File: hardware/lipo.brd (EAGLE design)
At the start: 33.5 x 34.6 mm, 50 parts, among them J1 MICRO_USB_B_HIROSE_ZX62-B-5PA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, Q1 IRLML6402, Q2 IRLML6344, SW1 TVAF06-A020B-R, U1 LT6106CS5#PBF, U2 NJM12888F, X1 FA-238

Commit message: べたGND前です。esp32のschはノータッチなのでここに上がってないです。よろしくお願いします。
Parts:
- moved C10 0.25 mm to (3.56, -3.81)
- moved C6 0.25 mm to (0.51, -3.81)
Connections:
- net VDD: now also RP1.26
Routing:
- net VDD: track 73.1 -> 74.6 mm, vias 6 -> 7
- net GND: vias 71 -> 67

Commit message: 微修正
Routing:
- net GND: track 155.3 -> 175.0 mm

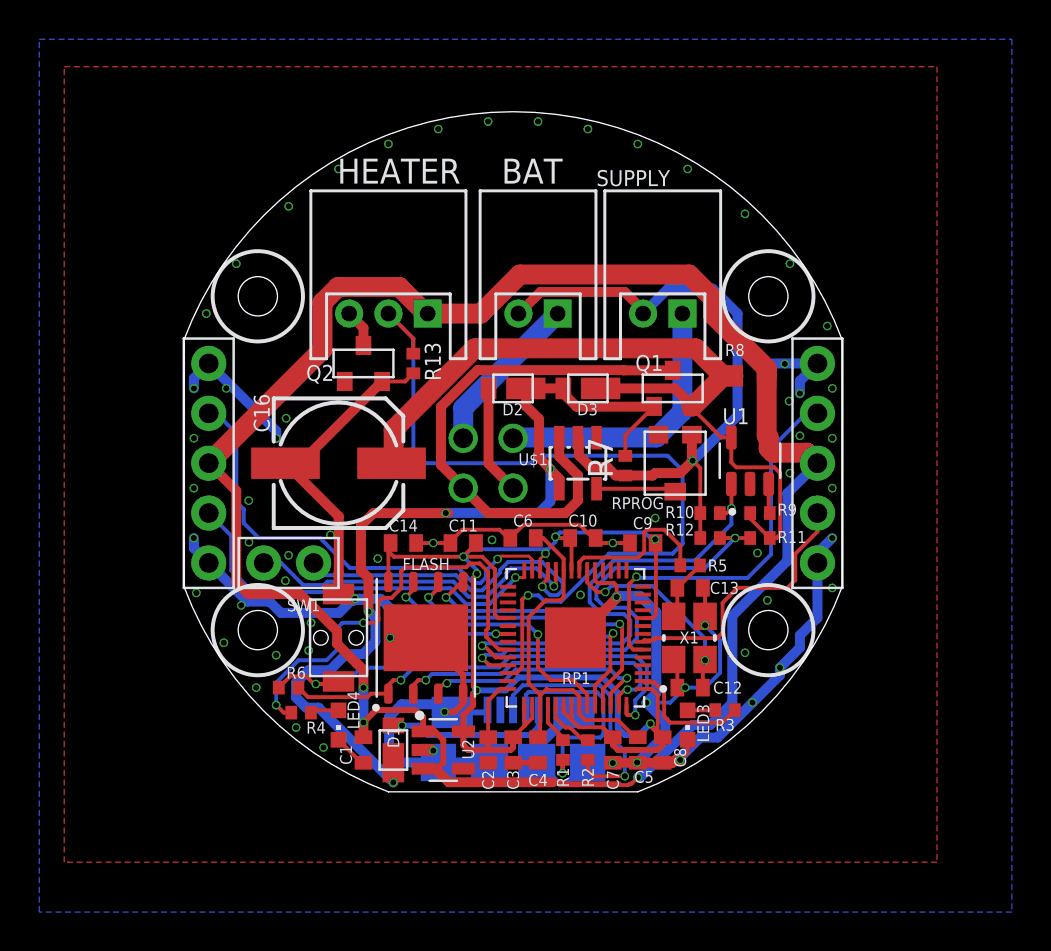
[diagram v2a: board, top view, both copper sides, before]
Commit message: シルクを調整
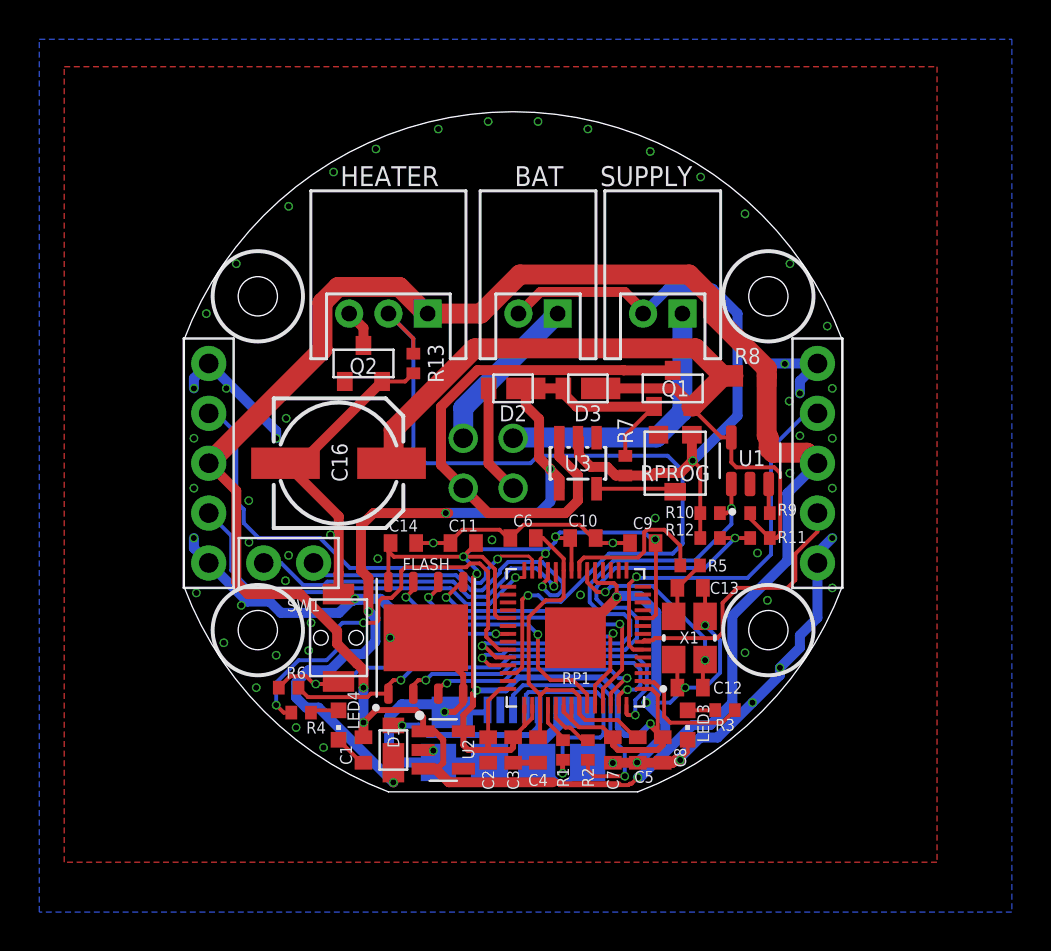
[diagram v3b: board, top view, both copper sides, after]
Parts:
- renumbered U$1 to U3
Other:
- board text added: "TERES LiPo Module"
- board text removed: "TERES Module"
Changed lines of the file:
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@@
 <layer number="27" name="tValues" color="7" fill="1" visible="yes" active="yes"/>
 <layer number="28" name="bValues" color="7" fill="1" visible="yes" active="yes"/>
-<layer number="29" name="tStop" color="7" fill="3" visible="no" active="yes"/>
-<layer number="30" name="bStop" color="7" fill="6" visible="no" active="yes"/>
+<layer number="29" name="tStop" color="7" fill="3" visible="yes" active="yes"/>
+<layer number="30" name="bStop" color="7" fill="6" visible="yes" active="yes"/>
 <layer number="31" name="tCream" color="7" fill="4" visible="no" active="yes"/>
 <layer number="32" name="bCream" color="7" fill="5" visible="no" active="yes"/>
@@
 <wire x1="-6.349996875" y1="-16.735815625" x2="-16.764" y2="-6.275209375" width="0" layer="20" curve="-48.699765"/>
 <wire x1="16.764" y1="-6.2752125" x2="6.35" y2="-16.7358125" width="0" layer="20" curve="-48.699745"/>
-<text x="0" y="14.859" size="1.27" layer="29" font="vector" ratio="10" align="center">2022 WASA Rocket</text>
-<text x="0" y="14.859" size="1.27" layer="30" font="vector" ratio="10" rot="MR0" align="center">TERES Module</text>
+<text x="0" y="16.002" size="1.016" layer="29" font="vector" ratio="10" align="center">2022 WASA Rocket</text>
+<text x="0.127" y="14.732" size="1.016" layer="30" font="vector" ratio="10" rot="MR0" align="center">TERES LiPo Module</text>
 <circle x="13" y="-8.5" radius="2.3" width="0.2" layer="22"/>
 <circle x="-13" y="-8.5" radius="2.3" width="0.2" layer="22"/>
@@
 <element name="U$2" library="pins" package="P2_2.54" value="P2_2_2.54" x="-11.43" y="-5.08" smashed="yes" rot="R90"/>
 <element name="BAT" library="jst-ph" package="S2B-PH-K-S" value="" x="1.27" y="7.62" smashed="yes">
-<attribute name="NAME" x="-0.587" y="14.239" size="1.27" layer="25" ratio="10"/>
+<attribute name="NAME" x="1.318" y="14.62" size="1.016" layer="25" font="vector" align="center"/>
 <attribute name="VALUE" x="-1.73" y="3.62" size="1.27" layer="27"/>
 </element>
-<element name="U$1" library="mcp73831" package="SOT23-5L" value="MCP73831" x="3.302" y="0" smashed="yes" rot="R180">
-<attribute name="NAME" x="1.778" y="0.508" size="0.6096" layer="25" font="vector" rot="R180"/>
+<element name="U3" library="mcp73831" package="SOT23-5L" value="MCP73831" x="3.302" y="0" smashed="yes" rot="R180">
+<attribute name="NAME" x="3.302" y="0" size="0.8128" layer="25" font="vector" rot="R180" align="center"/>
 </element>
 <element name="HEATER" library="jst-ph" package="S3B-PH-K-S" value="" x="-6.35" y="7.62" smashed="yes">
-<attribute name="NAME" x="-8.953" y="14.239" size="1.27" layer="25" ratio="10"/>
+<attribute name="NAME" x="-6.286" y="14.62" size="1.016" layer="25" font="vector" align="center"/>
 <attribute name="VALUE" x="-10.35" y="3.62" size="1.27" layer="27"/>
 </element>
 <element name="SUPPLY" library="jst-ph" package="S2B-PH-K-S" value="" x="7.62" y="7.62" smashed="yes">
-<attribute name="NAME" x="4.239" y="14.112" size="0.8128" layer="25" ratio="10"/>
+<attribute name="NAME" x="6.779" y="14.62" size="1.016" layer="25" font="vector" align="center"/>
 <attribute name="VALUE" x="4.62" y="3.62" size="1.27" layer="27"/>
 </element>
@@
 <attribute name="MF" value="Linear Technology" x="12.065" y="0.127" size="1.778" layer="27" rot="R90" display="off"/>
 <attribute name="MP" value="LT6106CS5#PBF" x="12.065" y="0.127" size="1.778" layer="27" rot="R90" display="off"/>
-<attribute name="NAME" x="12.033" y="2.799" size="0.8128" layer="25" rot="R180"/>
+<attribute name="NAME" x="12.16" y="0.259" size="0.8128" layer="25" font="vector" rot="R180" align="center"/>
 <attribute name="PACKAGE" value="TSOT-23 Linear Technology" x="12.065" y="0.127" size="1.778" layer="27" rot="R90" display="off"/>
 <attribute name="PRICE" value="None" x="12.065" y="0.127" size="1.778" layer="27" rot="R90" display="off"/>
 </element>
 <element name="D2" library="diodes" package="CUHS20S30" value="CUHS20S30" x="0" y="3.81" smashed="yes" rot="R180">
-<attribute name="NAME" x="0.508" y="3.048" size="0.6096" layer="25" font="vector" rot="R180"/>
+<attribute name="NAME" x="0" y="2.54" size="0.8128" layer="25" font="vector" rot="R180" align="center"/>
 </element>
 <element name="RPROG" library="potentiometers" package="PVZ3A" value="10k" x="8.255" y="0" smashed="yes" rot="R180">
-<attribute name="NAME" x="6.35" y="-2.032" size="0.6096" layer="25" font="vector" rot="R180" align="center"/>
+<attribute name="NAME" x="8.255" y="-0.508" size="0.8128" layer="25" font="vector" rot="R180" align="center"/>
 </element>
 <element name="Q1" library="mosfet" package="SOT-23" value="IRLML6402" x="8.128" y="3.81" smashed="yes">
-<attribute name="NAME" x="6.223" y="4.699" size="0.8128" layer="25" font="vector"/>
+<attribute name="NAME" x="8.255" y="3.81" size="0.8128" layer="25" font="vector" align="center"/>
 </element>
 <element name="D3" library="diodes" package="CUHS20S30" value="CUHS20S30" x="3.81" y="3.81" smashed="yes" rot="R180">
-<attribute name="NAME" x="4.318" y="3.048" size="0.6096" layer="25" font="vector" rot="R180"/>
+<attribute name="NAME" x="3.81" y="2.54" size="0.8128" layer="25" font="vector" rot="R180" align="center"/>
 </element>
 <element name="R7" library="rcl" library_urn="urn:adsk.eagle:library:334" package="R0402" package3d_urn="urn:adsk.eagle:package:23547/3" value="100k" x="5.715" y="-0.127" smashed="yes" rot="R90">
-<attribute name="NAME" x="5.08" y="-0.762" size="1.27" layer="25" rot="R90"/>
+<attribute name="NAME" x="5.715" y="1.651" size="0.8128" layer="25" font="vector" rot="R90" align="center"/>
 <attribute name="POPULARITY" value="34" x="5.715" y="-0.127" size="1.778" layer="27" rot="R90" display="off"/>
 <attribute name="SPICEPREFIX" value="R" x="5.715" y="-0.127" size="1.778" layer="27" rot="R90" display="off"/>
 </element>
 <element name="R8" library="rcl" library_urn="urn:adsk.eagle:library:334" package="R0603" package3d_urn="urn:adsk.eagle:package:23555/3" value="0.033" x="12.065" y="4.445" smashed="yes">
-<attribute name="NAME" x="10.795" y="5.461" size="0.6096" layer="25" font="vector"/>
+<attribute name="NAME" x="11.938" y="5.461" size="0.8128" layer="25" font="vector" align="center"/>
 <attribute name="POPULARITY" value="77" x="12.065" y="4.445" size="1.778" layer="27" display="off"/>
 <attribute name="SPICEPREFIX" value="R" x="12.065" y="4.445" size="1.778" layer="27" display="off"/>
@@
 </element>
 <element name="C16" library="rcl" library_urn="urn:adsk.eagle:library:334" package="153CLV-0605" package3d_urn="urn:adsk.eagle:package:23398/2" value="" x="-8.89" y="0" smashed="yes">
-<attribute name="NAME" x="-12.393" y="1.563" size="0.8128" layer="25" font="vector" rot="R90"/>
+<attribute name="NAME" x="-8.837" y="0.039" size="0.8128" layer="25" font="vector" rot="R90" align="center"/>
 <attribute name="POPULARITY" value="5" x="-8.89" y="0" size="1.778" layer="27" display="off"/>
 <attribute name="SPICEPREFIX" value="C" x="-8.89" y="0" size="1.778" layer="27" display="off"/>
@@
 </element>
 <element name="R13" library="rcl" library_urn="urn:adsk.eagle:library:334" package="R0402" package3d_urn="urn:adsk.eagle:package:23547/3" value="22k" x="-5.08" y="5.08" smashed="yes" rot="R90">
-<attribute name="NAME" x="-3.683" y="4.191" size="0.8128" layer="25" font="vector" rot="R90"/>
+<attribute name="NAME" x="-3.937" y="5.08" size="0.8128" layer="25" font="vector" rot="R90" align="center"/>
 <attribute name="POPULARITY" value="34" x="-5.08" y="5.08" size="1.778" layer="27" rot="R90" display="off"/>
 <attribute name="SPICEPREFIX" value="R" x="-5.08" y="5.08" size="1.778" layer="27" rot="R90" display="off"/>
 </element>
 <element name="Q2" library="mosfet" package="SOT-23" value="IRLML6344" x="-7.62" y="5.08" smashed="yes">
-<attribute name="NAME" x="-10.541" y="4.191" size="0.8128" layer="25" font="vector"/>
+<attribute name="NAME" x="-7.62" y="4.953" size="0.8128" layer="25" font="vector" align="center"/>
 </element>
 </elements>
@@
 <via x="14.097" y="10.16" extent="1-16" drill="0.3"/>
 <via x="11.811" y="12.7" extent="1-16" drill="0.3"/>
-<via x="8.89" y="14.986" extent="1-16" drill="0.3"/>
-<via x="6.35" y="16.256" extent="1-16" drill="0.3"/>
+<via x="9.5515" y="14.5765" extent="1-16" drill="0.3"/>
+<via x="6.985" y="15.875" extent="1-16" drill="0.3"/>
 <via x="3.81" y="17.018" extent="1-16" drill="0.3"/>
 <via x="1.27" y="17.399" extent="1-16" drill="0.3"/>
 <via x="-1.27" y="17.399" extent="1-16" drill="0.3"/>
 <via x="-3.81" y="17.018" extent="1-16" drill="0.3"/>
-<via x="-6.35" y="16.256" extent="1-16" drill="0.3"/>
-<via x="-8.89" y="14.986" extent="1-16" drill="0.3"/>
+<via x="-6.985" y="16.002" extent="1-16" drill="0.3"/>
+<via x="-9.142" y="14.8285" extent="1-16" drill="0.3"/>
 <via x="-14.097" y="10.16" extent="1-16" drill="0.3"/>
 <via x="-15.621" y="7.62" extent="1-16" drill="0.3"/>
@@
 <contactref element="BAT" pad="2"/>
 <contactref element="SUPPLY" pad="2"/>
-<contactref element="U$1" pad="2"/>
+<contactref element="U3" pad="2"/>
 <contactref element="RPROG" pad="1"/>
 <contactref element="R7" pad="1"/>
@@
 </signal>
 <signal name="CHARGE">
-<contactref element="U$1" pad="1"/>
+<contactref element="U3" pad="1"/>
 </signal>
 <signal name="VBAT">
-<contactref element="U$1" pad="3"/>
+<contactref element="U3" pad="3"/>
 <contactref element="Q1" pad="P3"/>
 <via x="-2.54" y="-1.27" extent="1-16" drill="1" diameter="1.5" alwaysstop="yes"/>
@@
 <signal name="N$4">
 <contactref element="RPROG" pad="2"/>
-<contactref element="U$1" pad="5"/>
+<contactref element="U3" pad="5"/>
 <wire x1="4.252" y1="-1.3" x2="8.105" y2="-1.3" width="0.2" layer="1"/>
 <wire x1="8.105" y1="-1.3" x2="8.255" y2="-1.45" width="0.2" layer="1"/>
@@
 <contactref element="D3" pad="A"/>
 <contactref element="R7" pad="2"/>
-<contactref element="U$1" pad="4"/>
+<contactref element="U3" pad="4"/>
 <wire x1="2.56" y1="3.81" x2="0.65" y2="3.81" width="0.508" layer="1"/>
 <wire x1="2.56" y1="3.81" x2="2.56" y2="3.554790625" width="0.508" layer="1"/>

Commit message: 若干修正
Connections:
- removed net N$7: U1.2
- net GND: now also U1.2
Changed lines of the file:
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@@
 <wire x1="-15.5" y1="5.08" x2="-12.065" y2="1.645" width="0.508" layer="16"/>
 <wire x1="-12.065" y1="1.645" x2="-12.065" y2="1.27" width="0.508" layer="16"/>
+<contactref element="U1" pad="2"/>
 </signal>
 <signal name="USB_DM">
@@
 <wire x1="-7.366" y1="-7.556" x2="-7.34964375" y2="-7.53964375" width="0" layer="19" extent="16-16"/>
 </signal>
-<signal name="N$7">
-<contactref element="U1" pad="2"/>
-</signal>
 <signal name="N$2">

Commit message: LiPo回路修正，新LoRa
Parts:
- removed D1, D2: CUHS20S30, diodes:CUHS20S30
- removed Q2: IRLML6344, mosfet:SOT-23
- added C15: 10µF, rcl:C0402
- added C18: 0.1µF, rcl:C0402
- added L1: 4.7µH, rcl:L3225M
- added R14: 100k, rcl:R0402
- added R15: 100, rcl:R0402
- added S1: SSAJ120100, SSAJ120100:SSAJ120100
- added U$1: TPS63000, TPS63000:10-VFDFN
- added U$3: S2B-ZR, con-jst-zh:S2B-ZR
- added U5: TCK106AF,LF, TCK106AF_LF:IC_TCK106AF,LF
- added VR1: 22k, potentiometers:PVZ3A
- C16: value (none) -> 10µF; device rcl:153CLV-0605 -> rcl:C0402
- R13: value 22k -> 10k
- moved C16 19.1 mm to (10.2, -1.65), turned to 270 degrees
- moved RPROG 9.58 mm to (-1.27, -1.02)
- moved BAT 9.09 mm to (-7.62, 5.71)
- moved U3 7.94 mm to (-4.57, -1.02)
- moved Q1 7.84 mm to (2.16, -1.27)
- moved HEATER 6.35 mm to (0.00, 7.62)
- moved R7 4.49 mm to (3.56, 3.81), turned to 0 degrees
- moved D3 4.32 mm to (0.00, 1.78)
- moved R8 3.20 mm to (12.4, 1.27)
- moved R10 2.57 mm to (10.9, -4.95), turned to 90 degrees
- moved R13 1.98 mm to (-3.56, 3.81), turned to 180 degrees
- moved SUPPLY 1.91 mm to (7.62, 5.71)
- moved U1 1.82 mm to (12.4, -1.65)
- moved R9 1.78 mm to (12.7, -4.32)
- moved R11 1.66 mm to (12.7, -5.46)
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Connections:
- net ISENSE renamed V+_I
- net VSENSE renamed BAT_V
- removed net N$10: HEATER.3, Q2.P3
- removed net N$6: D1.A, J1.VBUS
- removed net V: C16.+, D3.C, Q1.P2, R11.2, R8.1, R9.2, U1.5
- removed net VBAT_IN: BAT.1
- removed net VSUP: D2.A
- removed net VSUP_IN: SUPPLY.1
- new net EN: C18.1, S1.2, U$1.6, U$1.7, U$1.8, U$3.2
- new net N$1: L1.1, U$1.4
- new net N$13: HEATER.1, U5.1
- new net N$14: R15.2, S1.C, U$3.1
- new net N$3: C15.1, D3.C, Q1.P2, R15.1, U$1.5, U5.5
- new net N$7: L1.2, U$1.2
- new net SUPPLY_V: R14.2, R7.1
- new net V+_V: U$1.10, VR1.2
- new net VOUT: C16.1, R8.1, R9.2, U$1.1, U1.5, VR1.1
- net GND: now also C15.2, C16.2, C18.2, HEATER.2, R14.1, U$1.3, U$1.9, U$1.P$1, U$1.P$2, U$1.P$3, U$1.P$4, U$1.P$5, U5.2, VR1.3; no longer C16.-, Q2.P2, R13.1, R7.1
- net HEATER: now also U5.3; no longer Q2.P1
- net TEMP: now also HEATER.3, R13.1; no longer HEATER.2, R13.2
- net V+: no longer HEATER.1
- net VBAT: now also BAT.1, R11.2
- net VDD: now also R13.2
- net VPP: now also J1.VBUS, SUPPLY.1; no longer D1.C, D2.C
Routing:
- net GND: track 175.0 -> 117.5 mm
- net V+: track 102.0 -> 57.7 mm
- net V: track 41.3 -> 0.00 mm
- net VPP: track 47.6 -> 8.19 mm, vias 4 -> 3
- net TEMP: track 42.2 -> 4.68 mm
- net VBAT: track 27.4 -> 0.00 mm, vias 1 -> 0
- net VSUP_IN: track 14.2 -> 0.00 mm, vias 1 -> 0
- net N$6: track 8.64 -> 0.00 mm, vias 1 -> 0
- net VBAT_IN: track 8.34 -> 0.00 mm, vias 1 -> 0
- net VSUP: track 5.60 -> 0.00 mm, vias 1 -> 0
- net N$4: track 4.07 -> 0.00 mm
- net V+_I: track 24.7 -> 22.5 mm
- net BAT_V: track 23.5 -> 21.5 mm
- net N$10: track 1.92 -> 0.00 mm
- net N$2: track 1.51 -> 0.00 mm

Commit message: アナログ入力を修正
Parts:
- added IC1, IC2: 4066D, 40xx:SO14
- added NTC: 10k, rcl:R0603
- added R16: 0.033, rcl:R0603
- added R17: 10k, rcl:R0402
- moved R15 1.09 mm to (-3.17, 3.56)
- moved R13 0.97 mm to (-3.17, 4.70)
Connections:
- removed net ADC3: RP1.41
- removed net I2C0_SDA: RP1.11
- removed net I2C1_SCL: RP1.9
- removed net I2C1_SDA: RP1.8
- removed net I2C_SCL: RP1.12
- removed net PWM0_B: RP1.3
- removed net PWM1_A: RP1.4
- removed net PWM1_B: RP1.5
- removed net PWM3_A: RP1.34
- removed net PWM4_A: RP1.36
- removed net PWM5_A: RP1.13
- removed net PWM5_B: RP1.14
- removed net SPI0_CS: RP1.32
- removed net SPI0_MISO: RP1.31
- removed net SPI0_MOSI: RP1.30
- removed net SPI0_SCK: RP1.29
- removed net SPI1_CS: RP1.16
- removed net SPI1_MISO: RP1.15
- removed net SPI1_MOSI: RP1.18
- removed net SPI1_SCK: RP1.17
- new net ADC0_IN: IC1.2, IC1.3, RP1.38
- new net ADC1_IN: IC1.10, IC1.9, RP1.39
- new net ADC2_IN: IC2.2, IC2.3, IC2.9, RP1.40
- new net ADC_SEL1: IC1.13, IC1.6, IC2.13
- new net ADC_SEL2: IC1.12, IC1.5, IC2.5
- new net ADC_SEL3: IC2.6
- new net HEATER_I: HEATER.2, IC1.11, R16.2
- new net OB_TEMP: IC2.8, NTC.2, R17.1
- new net VSS: IC1.7, IC2.7
- net BAT_V: now also IC1.4; no longer RP1.39
- net GND: now also NTC.1, R16.1; no longer HEATER.2
- net SUPPLY_V: now also IC1.1
- net TEMP: now also IC2.4; no longer RP1.40
- net V+_I: now also IC1.8; no longer RP1.38
- net V+_V: now also IC2.1
- net VDD: now also IC1.14, IC2.14, R17.2
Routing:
- net TEMP: track 4.68 -> 0.00 mm, vias 1 -> 0
- net GND: track 117.5 -> 119.6 mm, vias 67 -> 64
- net BAT_V: track 21.5 -> 20.5 mm
